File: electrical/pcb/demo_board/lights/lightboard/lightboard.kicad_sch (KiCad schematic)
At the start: 32 parts, among them J1 Conn_01x06_Pin, J2 Conn_01x06_Pin

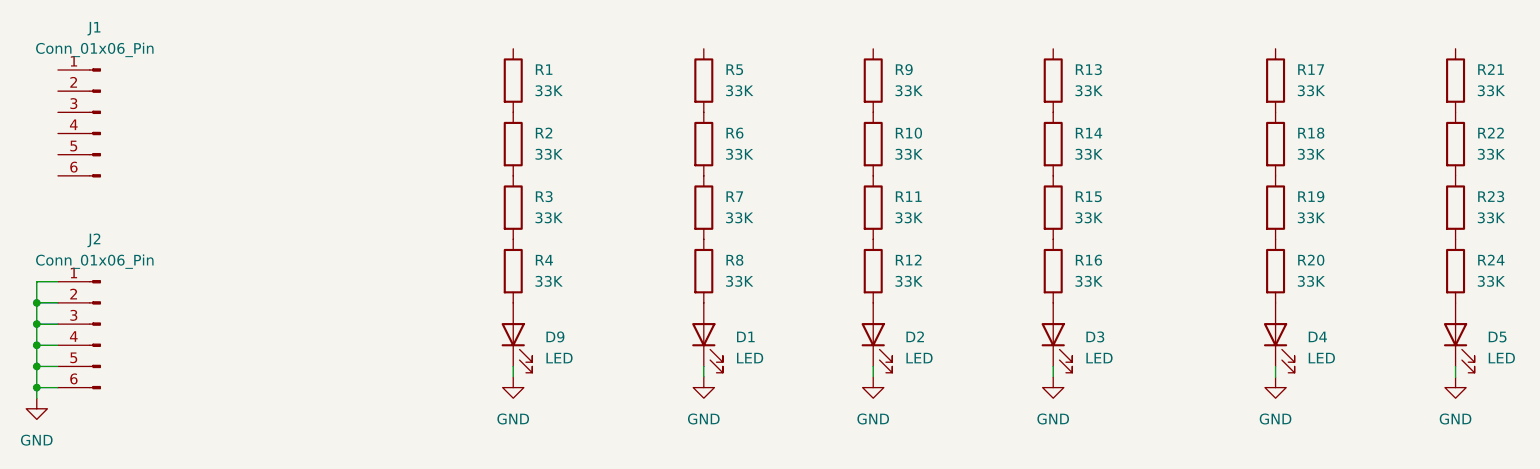
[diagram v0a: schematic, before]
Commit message: ordered boards
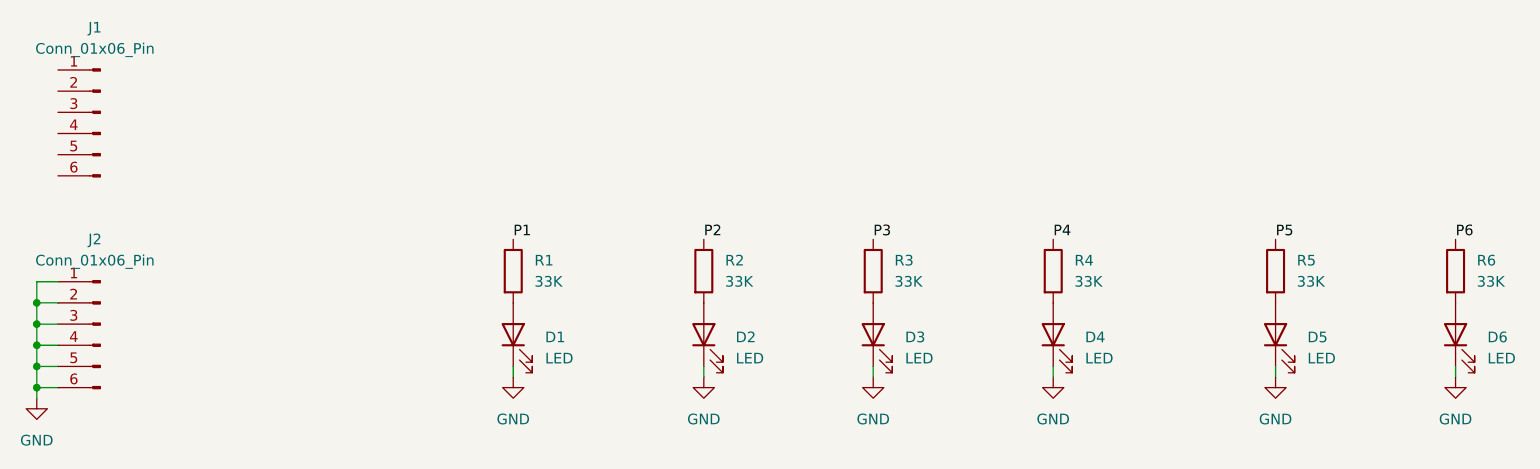
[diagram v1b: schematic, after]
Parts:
- removed R1, R10, R11, R13, R14, R15, R17, R18, R19, R2, R21, R22, R23, R3, R5, R6, R7, R9: 33K, Resistor_SMD:R_0603_1608Metric, symbol Device:R
- R1: renamed from R4; footprint Resistor_SMD:R_0603_1608Metric -> Resistor_SMD:R_1210_3225Metric
- R2: renamed from R8; footprint Resistor_SMD:R_0603_1608Metric -> Resistor_SMD:R_1210_3225Metric
- R3: renamed from R12; footprint Resistor_SMD:R_0603_1608Metric -> Resistor_SMD:R_1210_3225Metric
- R4: renamed from R16; footprint Resistor_SMD:R_0603_1608Metric -> Resistor_SMD:R_1210_3225Metric
- R5: renamed from R20; footprint Resistor_SMD:R_0603_1608Metric -> Resistor_SMD:R_1210_3225Metric
- R6: renamed from R24; footprint Resistor_SMD:R_0603_1608Metric -> Resistor_SMD:R_1210_3225Metric
- renumbered D9 to D1, D1 to D2, D2 to D3, D3 to D4, D4 to D5, D5 to D6
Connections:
- net P5: now reaches R5.1
- net P3: now reaches R3.1
- net P2: now reaches R2.1
- net P6: now reaches R6.1
- net P4: now reaches R4.1
- net P1: now reaches R1.1
